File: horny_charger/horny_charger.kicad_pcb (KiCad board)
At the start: 2 copper layers, 19.3 x 60.9 mm, 16 parts, among them J1 USB_C_Receptacle, SW1 SW_DPST_x2, U1 MCP73831-2-OT

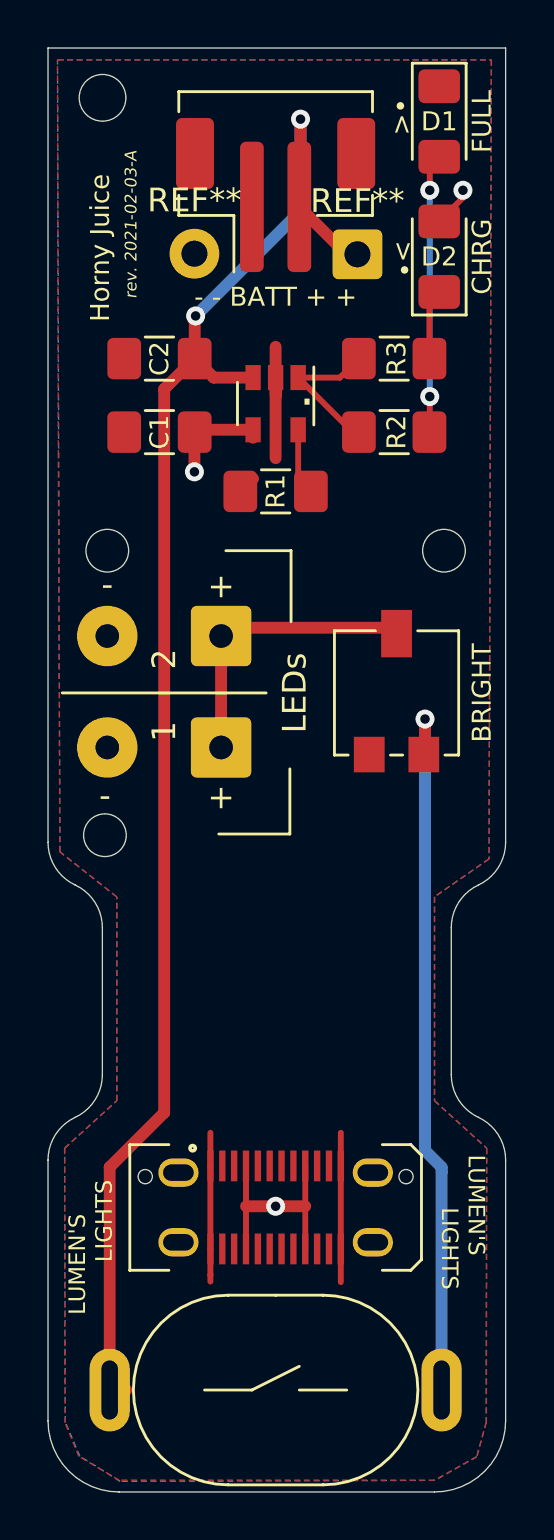
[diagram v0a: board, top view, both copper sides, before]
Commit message: upgrade to kicad6
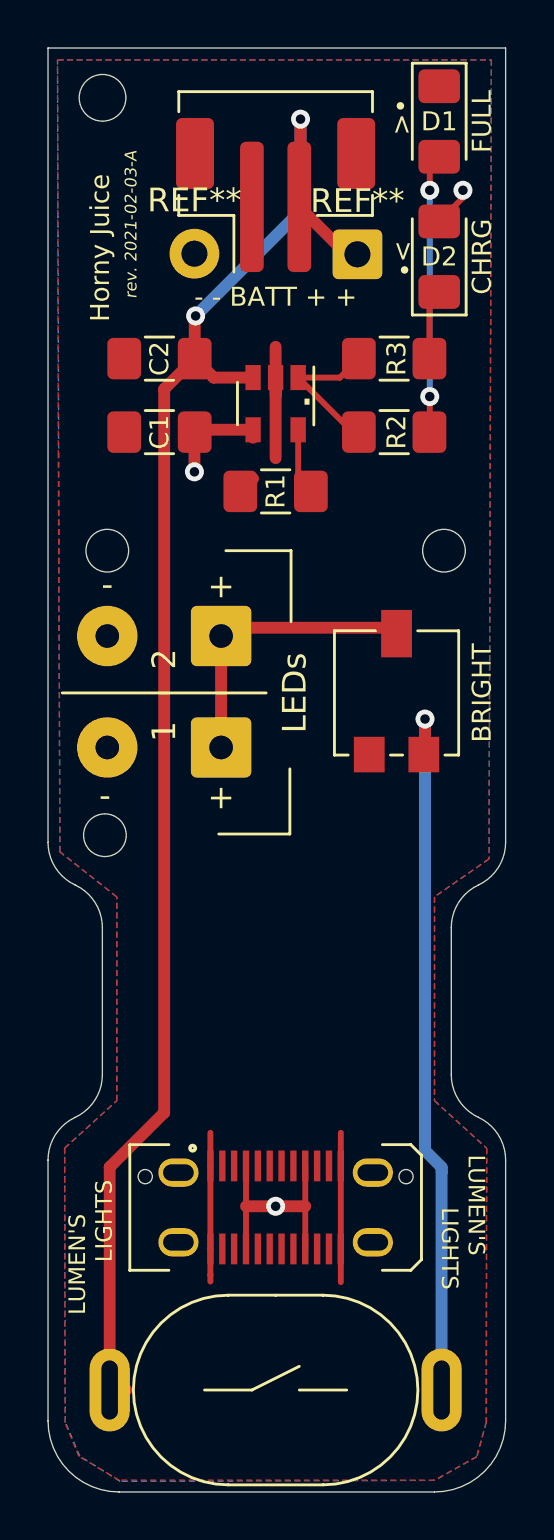
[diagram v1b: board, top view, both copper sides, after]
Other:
- net class Default removed
